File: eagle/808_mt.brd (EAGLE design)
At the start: 100.8 x 80.8 mm, 59 parts, among them IC1 TL071P, IC2 TL072P, Q1 2N3904, Q2 2N3906, Q3 2N3904, SW8 808_LT_MSS42_SW_4PDT

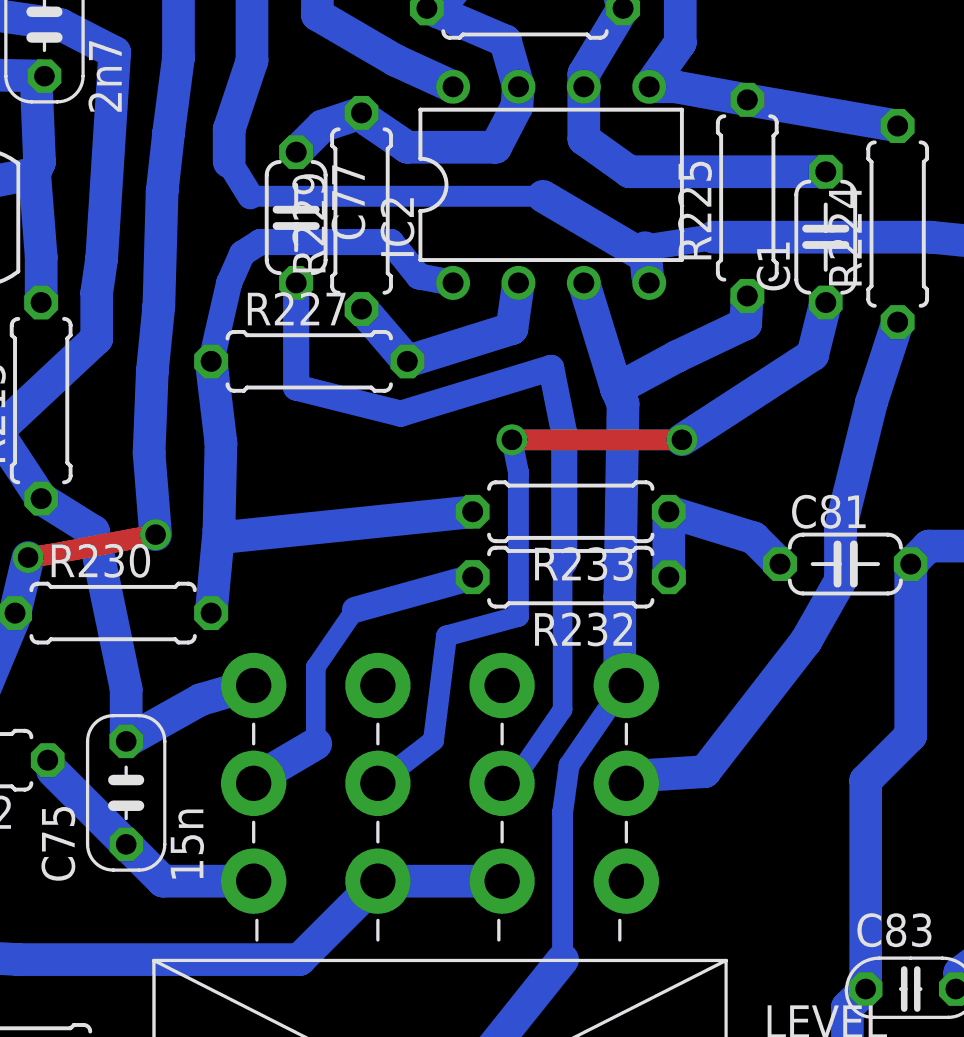
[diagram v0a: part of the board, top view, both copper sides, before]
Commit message: changed values for hitom
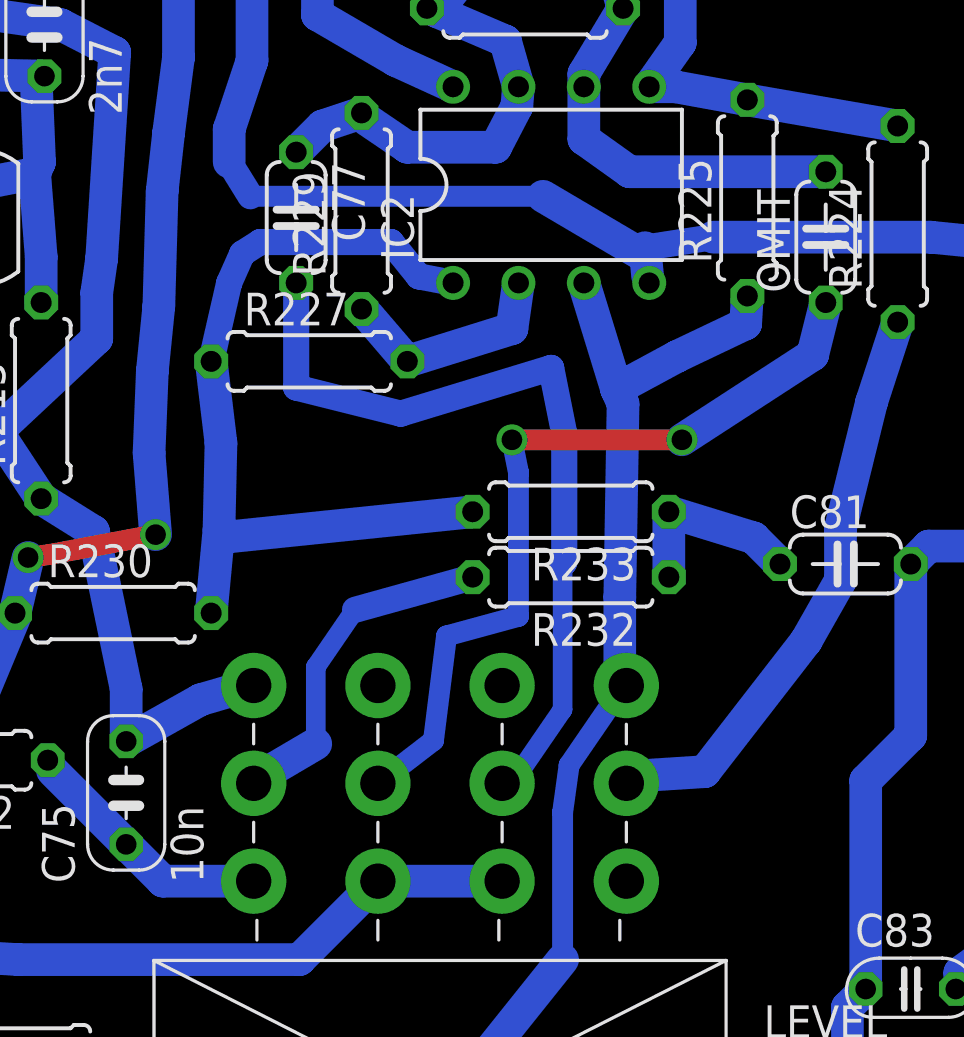
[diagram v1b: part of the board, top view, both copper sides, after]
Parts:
- C74: value 33n -> 27n
- C75: value 15n -> 10n
- C77: value 27n -> 22n
- C78: value 12n -> 5n6
- C81: value 39n -> 33n
- OMIT: value 8n2 -> OMIT
- R224: value 2k2 -> 1k5
- R225: value 6k8 -> 5k6
- renumbered C1 to OMIT
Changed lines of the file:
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@@
 <?xml version="1.0" encoding="utf-8"?>
 <!DOCTYPE eagle SYSTEM "eagle.dtd">
-<eagle version="7.1.0">
+<eagle version="7.2.0">
 <drawing>
 <settings>
@@
 <element name="C72" library="TR808clone" package="C050-024X044" value="33n" x="11.43" y="34.29" rot="R270"/>
 <element name="C73" library="TR808clone" package="C035-030X60" value="2n7" x="34.417" y="48.895" rot="R90"/>
-<element name="C74" library="TR808clone" package="C050-024X044" value="33n" x="27.432" y="31.75" rot="R270"/>
-<element name="C75" library="TR808clone" package="C035-030X60" value="15n" x="37.592" y="19.05" rot="R90"/>
+<element name="C74" library="TR808clone" package="C050-024X044" value="27n" x="27.432" y="31.75" rot="R270"/>
+<element name="C75" library="TR808clone" package="C035-030X60" value="10n" x="37.592" y="19.05" rot="R90"/>
 <element name="C76" library="TR808clone" package="C050-024X044" value="27n" x="56.388" y="53.848" rot="R90"/>
-<element name="C77" library="TR808clone" package="C050-024X044" value="27n" x="44.196" y="41.402" rot="R270"/>
-<element name="C78" library="TR808clone" package="C035-025X75" value="12n" x="51.562" y="54.356" rot="R270"/>
-<element name="C81" library="TR808clone" package="C050-024X044" value="39n" x="65.532" y="27.94"/>
+<element name="C77" library="TR808clone" package="C050-024X044" value="22n" x="44.196" y="41.402" rot="R270"/>
+<element name="C78" library="TR808clone" package="C035-025X75" value="5n6" x="51.562" y="54.356" rot="R270"/>
+<element name="C81" library="TR808clone" package="C050-024X044" value="33n" x="65.532" y="27.94"/>
 <element name="C82" library="TR808clone" package="E2-5" value="33/6.3" x="76.962" y="15.24" rot="R270"/>
 <element name="C83" library="TR808clone" package="C035-025X75" value="1n" x="68.072" y="11.43"/>
@@
 <element name="R222" library="TR808clone" package="0207/7" value="22K" x="30.734" y="20.32" rot="R180"/>
 <element name="R223" library="TR808clone" package="0207/7" value="22K" x="31.242" y="31.75" rot="R90"/>
-<element name="R224" library="TR808clone" package="0207/7" value="2k2" x="67.564" y="41.148" rot="R90"/>
-<element name="R225" library="TR808clone" package="0207/7" value="6k8" x="61.722" y="42.164" rot="R90"/>
+<element name="R224" library="TR808clone" package="0207/7" value="1k5" x="67.564" y="41.148" rot="R90"/>
+<element name="R225" library="TR808clone" package="0207/7" value="5k6" x="61.722" y="42.164" rot="R90"/>
 <element name="R226" library="TR808clone" package="0207/7" value="22K" x="43.942" y="55.118" rot="R180"/>
 <element name="R227" library="TR808clone" package="0207/7" value="33K" x="44.704" y="35.814"/>
@@
 <element name="TRIGGER" library="solpad" package="LSP10" value="LSP10" x="10.16" y="44.45"/>
 <element name="ACCENT" library="solpad" package="LSP10" value="LSP10" x="20.828" y="49.784"/>
-<element name="C1" library="TR808clone" package="C050-024X044" value="8n2" x="64.77" y="40.64" rot="R90"/>
+<element name="OMIT" library="TR808clone" package="C050-024X044" value="OMIT" x="64.77" y="40.64" rot="R90"/>
 </elements>
 <signals>
@@
 <wire x1="56.896" y1="49.53" x2="55.372" y2="46.99" width="1.27" layer="16"/>
 <wire x1="56.896" y1="49.53" x2="56.388" y2="51.308" width="1.27" layer="16"/>
-<contactref element="C1" pad="2"/>
+<contactref element="OMIT" pad="2"/>
 <wire x1="64.77" y1="43.18" x2="57.15" y2="43.18" width="1.27" layer="16"/>
 <wire x1="57.15" y1="43.18" x2="55.372" y2="44.45" width="1.27" layer="16"/>
@@
 <signal name="N$7">
 <contactref element="SW8" pad="P$5"/>
-<contactref element="C1" pad="1"/>
+<contactref element="OMIT" pad="1"/>
 <wire x1="47.371" y1="19.421" x2="49.53" y2="21.082" width="0.8128" layer="16"/>
 <wire x1="49.53" y1="21.082" x2="50.038" y2="25.146" width="0.8128" layer="16"/>

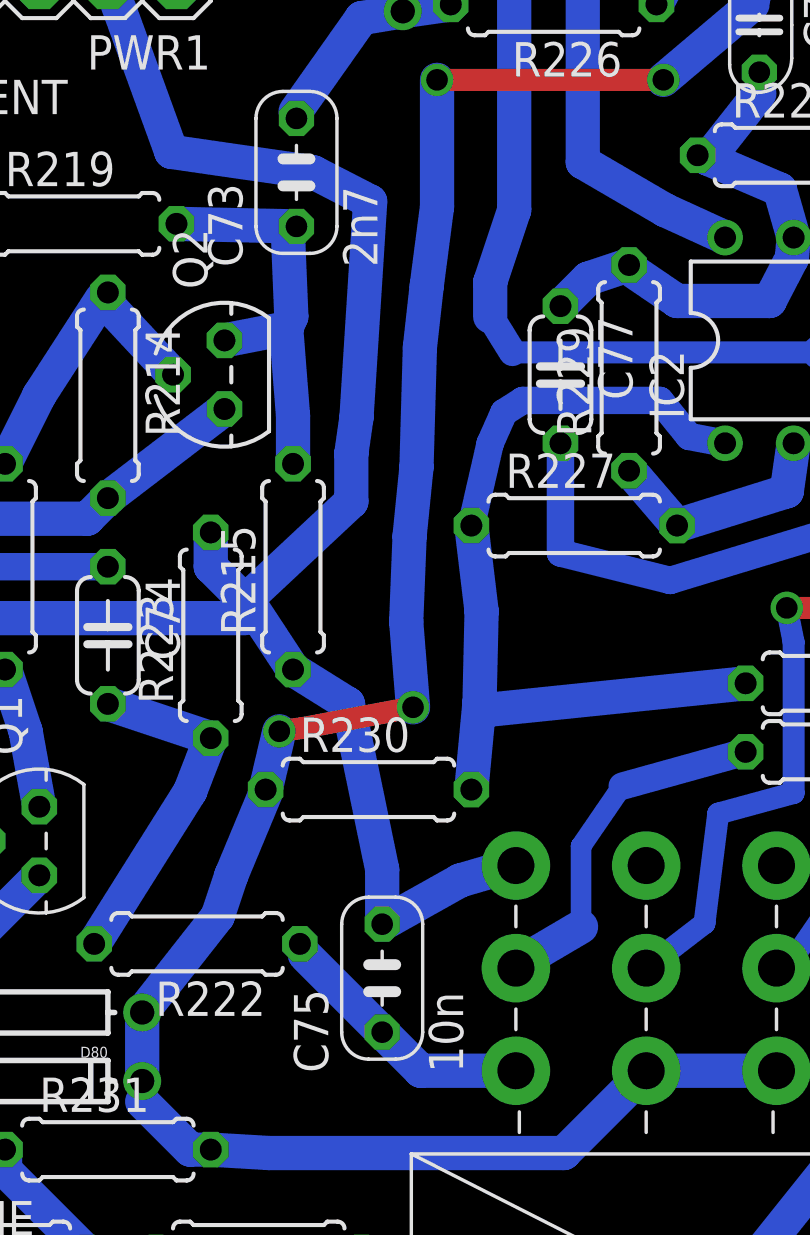
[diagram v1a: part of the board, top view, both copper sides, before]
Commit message: values for low tom
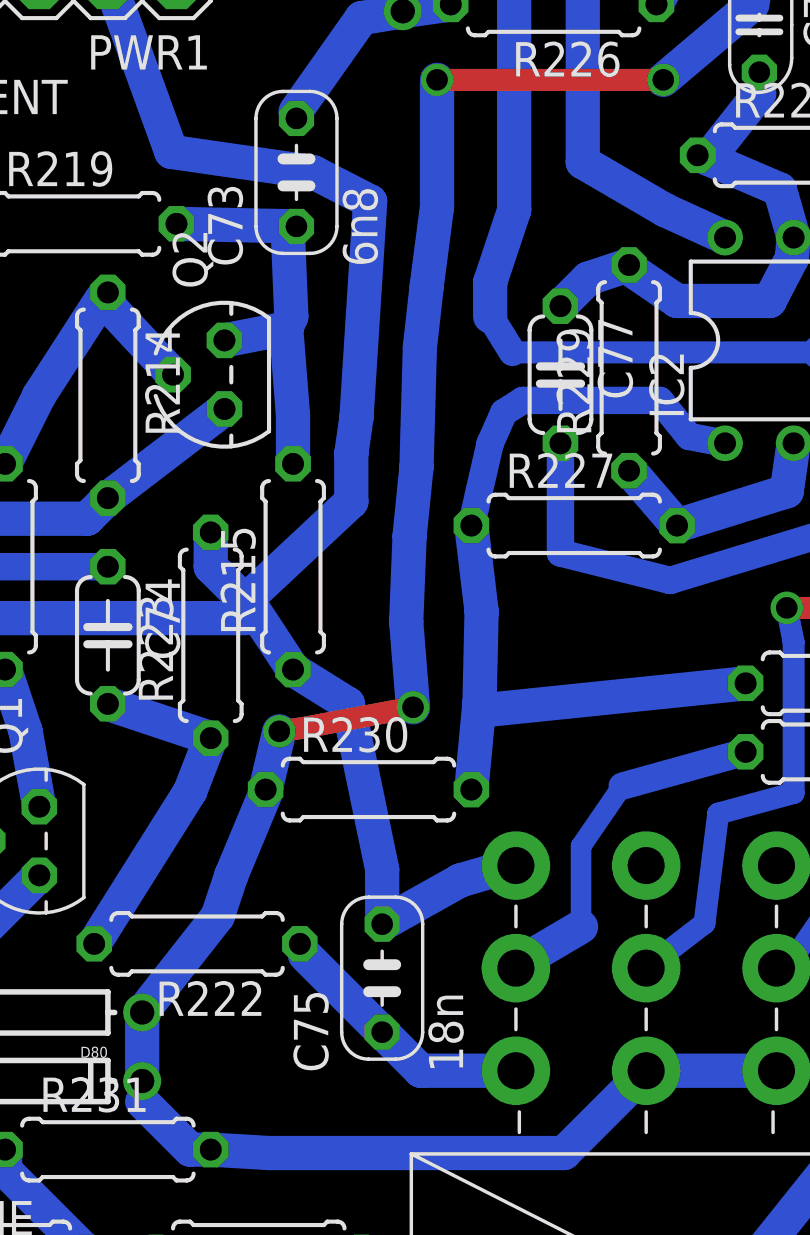
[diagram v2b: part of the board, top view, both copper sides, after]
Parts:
- C72: value 33n -> 39n
- C73: value 2n7 -> 6n8
- C74: value 27n -> 47n
- C75: value 10n -> 18n
- C76: value 27n -> 56n
- C77: value 22n -> 47n
- C78: value 5n6 -> 12n
- C81: value 33n -> 47n
- R225: value 5k6 -> 4k7
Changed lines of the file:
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@@
 <?xml version="1.0" encoding="utf-8"?>
 <!DOCTYPE eagle SYSTEM "eagle.dtd">
-<eagle version="7.2.0">
+<eagle version="7.1.0">
 <drawing>
 <settings>
@@
 <elements>
 <element name="C71" library="TR808clone" package="C050-024X044" value="47n" x="11.684" y="25.4" rot="R180"/>
-<element name="C72" library="TR808clone" package="C050-024X044" value="33n" x="11.43" y="34.29" rot="R270"/>
-<element name="C73" library="TR808clone" package="C035-030X60" value="2n7" x="34.417" y="48.895" rot="R90"/>
-<element name="C74" library="TR808clone" package="C050-024X044" value="27n" x="27.432" y="31.75" rot="R270"/>
-<element name="C75" library="TR808clone" package="C035-030X60" value="10n" x="37.592" y="19.05" rot="R90"/>
-<element name="C76" library="TR808clone" package="C050-024X044" value="27n" x="56.388" y="53.848" rot="R90"/>
-<element name="C77" library="TR808clone" package="C050-024X044" value="22n" x="44.196" y="41.402" rot="R270"/>
-<element name="C78" library="TR808clone" package="C035-025X75" value="5n6" x="51.562" y="54.356" rot="R270"/>
-<element name="C81" library="TR808clone" package="C050-024X044" value="33n" x="65.532" y="27.94"/>
+<element name="C72" library="TR808clone" package="C050-024X044" value="39n" x="11.43" y="34.29" rot="R270"/>
+<element name="C73" library="TR808clone" package="C035-030X60" value="6n8" x="34.417" y="48.895" rot="R90"/>
+<element name="C74" library="TR808clone" package="C050-024X044" value="47n" x="27.432" y="31.75" rot="R270"/>
+<element name="C75" library="TR808clone" package="C035-030X60" value="18n" x="37.592" y="19.05" rot="R90"/>
+<element name="C76" library="TR808clone" package="C050-024X044" value="56n" x="56.388" y="53.848" rot="R90"/>
+<element name="C77" library="TR808clone" package="C050-024X044" value="47n" x="44.196" y="41.402" rot="R270"/>
+<element name="C78" library="TR808clone" package="C035-025X75" value="12n" x="51.562" y="54.356" rot="R270"/>
+<element name="C81" library="TR808clone" package="C050-024X044" value="47n" x="65.532" y="27.94"/>
 <element name="C82" library="TR808clone" package="E2-5" value="33/6.3" x="76.962" y="15.24" rot="R270"/>
 <element name="C83" library="TR808clone" package="C035-025X75" value="1n" x="68.072" y="11.43"/>
@@
 <element name="R223" library="TR808clone" package="0207/7" value="22K" x="31.242" y="31.75" rot="R90"/>
 <element name="R224" library="TR808clone" package="0207/7" value="1k5" x="67.564" y="41.148" rot="R90"/>
-<element name="R225" library="TR808clone" package="0207/7" value="5k6" x="61.722" y="42.164" rot="R90"/>
+<element name="R225" library="TR808clone" package="0207/7" value="4k7" x="61.722" y="42.164" rot="R90"/>
 <element name="R226" library="TR808clone" package="0207/7" value="22K" x="43.942" y="55.118" rot="R180"/>
 <element name="R227" library="TR808clone" package="0207/7" value="33K" x="44.704" y="35.814"/>
